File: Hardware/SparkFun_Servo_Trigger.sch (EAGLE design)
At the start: 30 parts, among them U1 ATTINY84, Y1 16MHZ

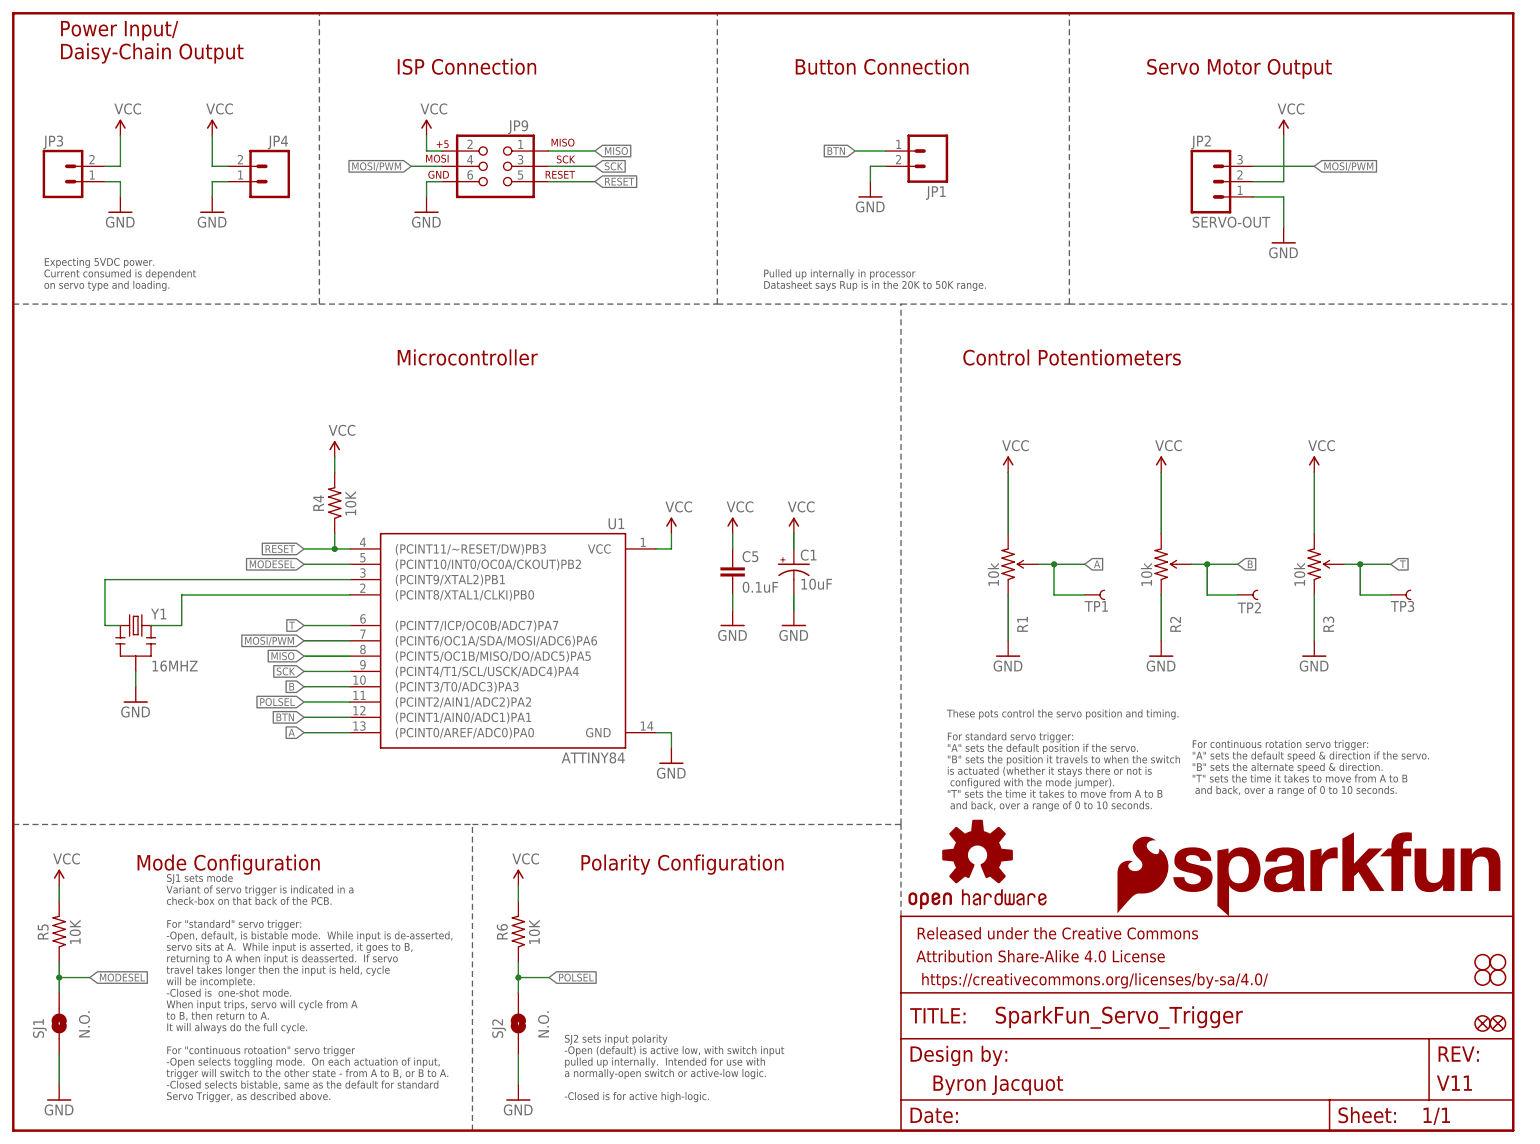
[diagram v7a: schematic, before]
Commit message: Updating logos from library.
Using rounded-corner versions to save CAM time.
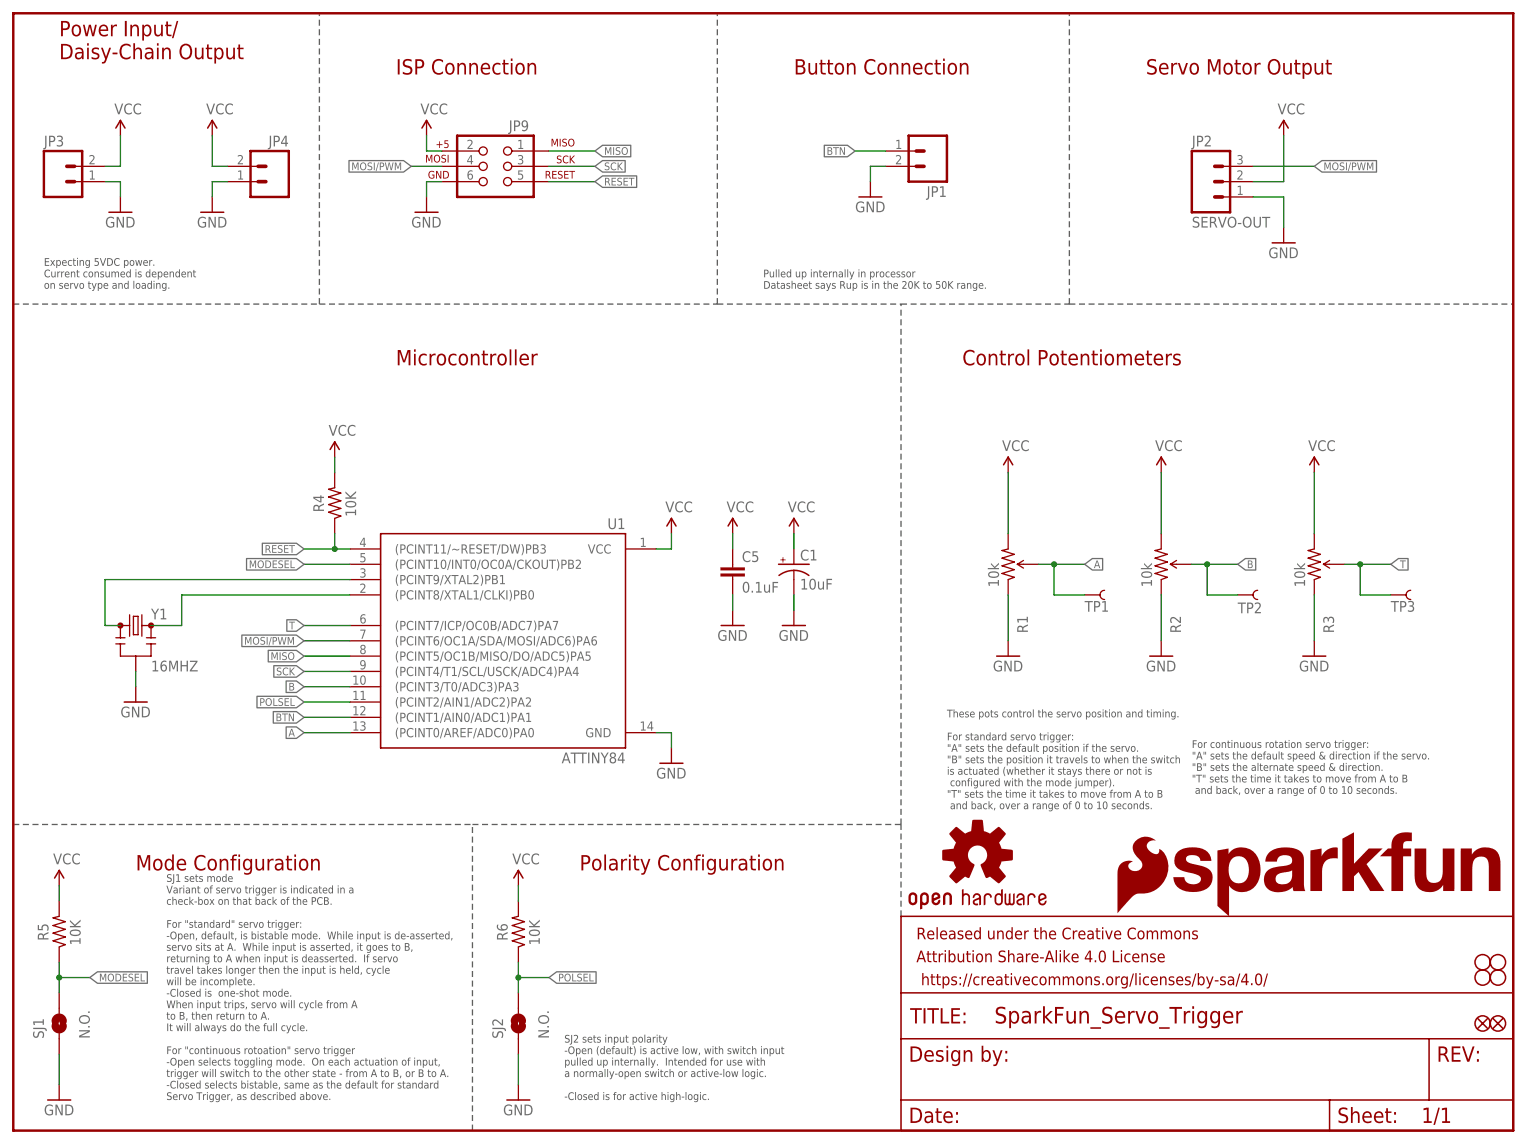
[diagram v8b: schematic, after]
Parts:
- FRAME1: DESIGNER Byron Jacquot -> (none); VERSION V11 -> (none)
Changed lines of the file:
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@@
 <layer number="56" name="wert" color="7" fill="1" visible="no" active="no"/>
 <layer number="57" name="tCAD" color="7" fill="1" visible="no" active="no"/>
+<layer number="59" name="tCarbon" color="7" fill="1" visible="no" active="no"/>
+<layer number="60" name="bCarbon" color="7" fill="1" visible="no" active="no"/>
 <layer number="90" name="Modules" color="5" fill="1" visible="yes" active="yes"/>
 <layer number="91" name="Nets" color="2" fill="1" visible="yes" active="yes"/>
@@
 <layer number="112" name="tSilk" color="7" fill="1" visible="yes" active="yes"/>
 <layer number="113" name="IDFDebug" color="4" fill="1" visible="no" active="yes"/>
+<layer number="114" name="Badge_Outline" color="7" fill="1" visible="yes" active="yes"/>
+<layer number="115" name="ReferenceISLANDS" color="7" fill="1" visible="yes" active="yes"/>
 <layer number="116" name="Patch_BOT" color="9" fill="4" visible="yes" active="yes"/>
+<layer number="118" name="Rect_Pads" color="7" fill="1" visible="yes" active="yes"/>
 <layer number="121" name="_tsilk" color="7" fill="1" visible="yes" active="yes"/>
 <layer number="122" name="_bsilk" color="7" fill="1" visible="yes" active="yes"/>
@@
 <layer number="127" name="_tValues" color="7" fill="1" visible="yes" active="yes"/>
 <layer number="128" name="_bValues" color="7" fill="1" visible="yes" active="yes"/>
+<layer number="129" name="Mask" color="7" fill="1" visible="yes" active="yes"/>
 <layer number="131" name="tAdjust" color="7" fill="1" visible="yes" active="yes"/>
 <layer number="132" name="bAdjust" color="7" fill="1" visible="yes" active="yes"/>
@@
 <layer number="223" name="223bmp" color="24" fill="1" visible="no" active="no"/>
 <layer number="224" name="224bmp" color="25" fill="1" visible="no" active="no"/>
+<layer number="225" name="225bmp" color="7" fill="1" visible="yes" active="yes"/>
+<layer number="226" name="226bmp" color="7" fill="1" visible="yes" active="yes"/>
+<layer number="227" name="227bmp" color="7" fill="1" visible="yes" active="yes"/>
+<layer number="228" name="228bmp" color="7" fill="1" visible="yes" active="yes"/>
+<layer number="229" name="229bmp" color="7" fill="1" visible="yes" active="yes"/>
+<layer number="230" name="230bmp" color="7" fill="1" visible="yes" active="yes"/>
+<layer number="231" name="231bmp" color="7" fill="1" visible="yes" active="yes"/>
 <layer number="248" name="Housing" color="7" fill="1" visible="yes" active="yes"/>
 <layer number="249" name="Edge" color="7" fill="1" visible="yes" active="yes"/>
@@
 </classes>
 <parts>
-<part name="FRAME1" library="SparkFun-Aesthetics" deviceset="FRAME-LETTER" device="" value="frame">
-<attribute name="DESIGNER" value="Byron Jacquot"/>
-<attribute name="VERSION" value="V11"/>
-</part>
+<part name="FRAME1" library="SparkFun-Aesthetics" deviceset="FRAME-LETTER" device="" value="frame"/>
 <part name="R4" library="SparkFun-Resistors" deviceset="10KOHM-1/10W-1%(0603)" device="0603" value="10K"/>
 <part name="JP9" library="SparkFun-Connectors" deviceset="AVR_SPI_PRG_6" device="PTH" value=""/>
@@
 <attribute name="NAME" x="154.94" y="156.718" size="1.778" layer="95" rot="R180"/>
 </instance>
-<instance part="JP2" gate="G$1" x="198.12" y="157.48"/>
+<instance part="JP2" gate="J$1" x="198.12" y="157.48"/>
 <instance part="GND4" gate="1" x="142.24" y="154.94"/>
 <instance part="GND5" gate="1" x="210.82" y="147.32"/>
@@
 </segment>
 <segment>
-<pinref part="JP2" gate="G$1" pin="2"/>
+<pinref part="JP2" gate="J$1" pin="2"/>
 <pinref part="SUPPLY9" gate="G$1" pin="VCC"/>
 <wire x1="205.74" y1="157.48" x2="210.82" y2="157.48" width="0.1524" layer="91"/>
@@
 </segment>
 <segment>
-<pinref part="JP2" gate="G$1" pin="1"/>
+<pinref part="JP2" gate="J$1" pin="1"/>
 <pinref part="GND5" gate="1" pin="GND"/>
 <wire x1="205.74" y1="154.94" x2="210.82" y2="154.94" width="0.1524" layer="91"/>
@@
 </segment>
 <segment>
-<pinref part="JP2" gate="G$1" pin="3"/>
+<pinref part="JP2" gate="J$1" pin="3"/>
 <wire x1="205.74" y1="160.02" x2="215.9" y2="160.02" width="0.1524" layer="91"/>
 <label x="215.9" y="160.02" size="1.27" layer="95" xref="yes"/>
